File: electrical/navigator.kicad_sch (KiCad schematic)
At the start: 10 parts

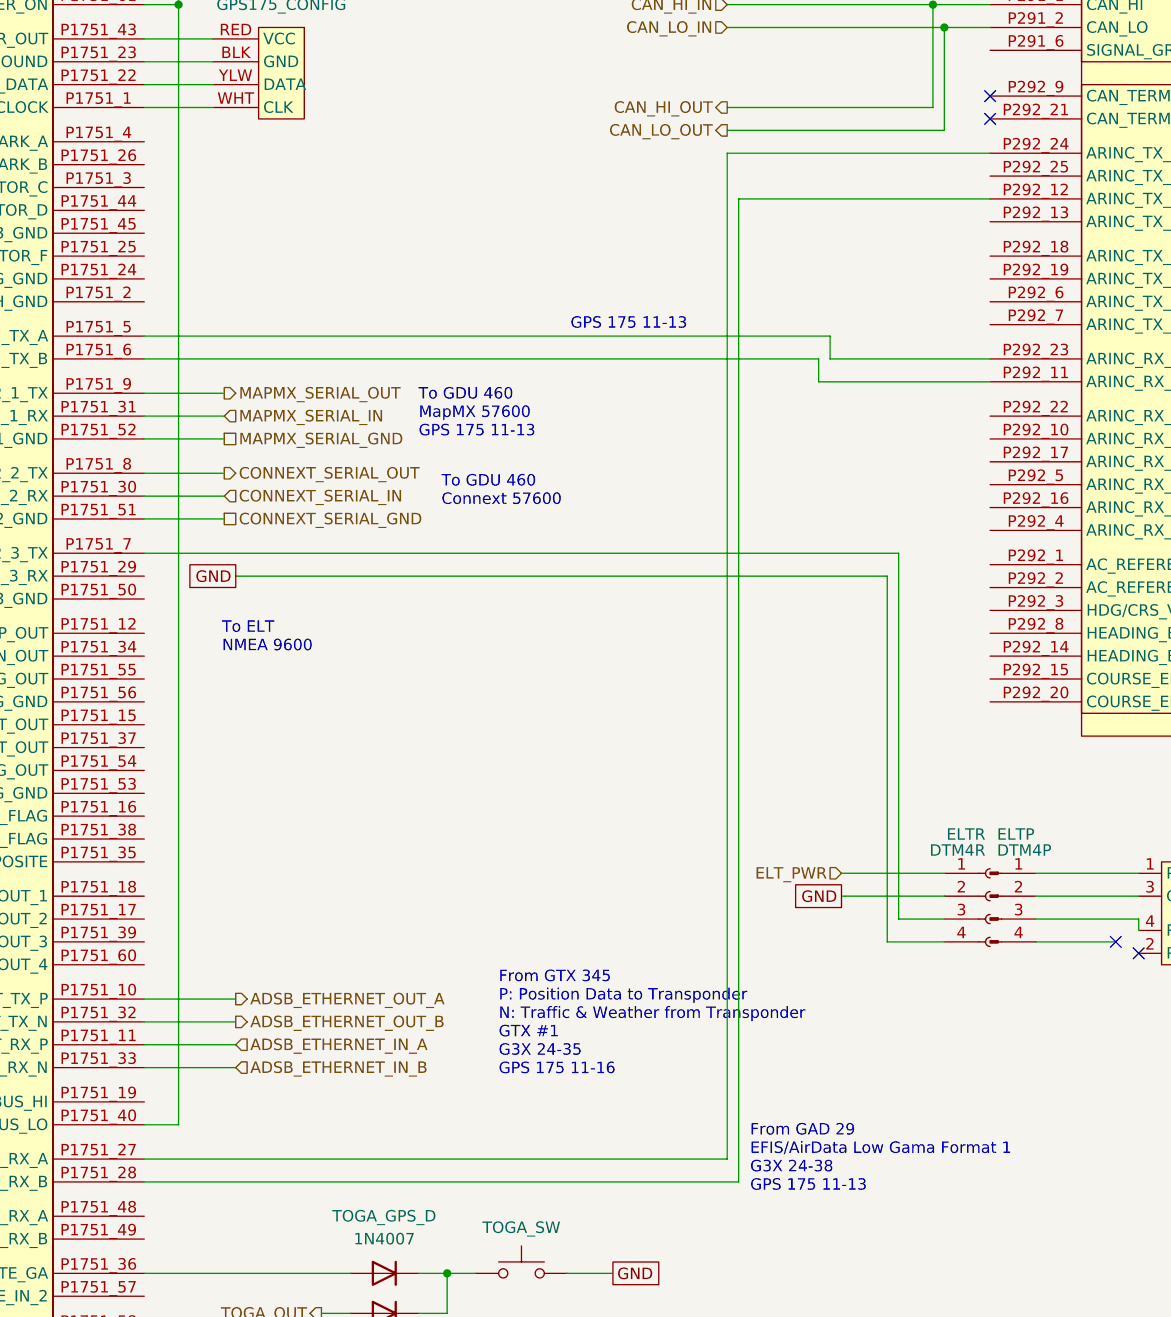
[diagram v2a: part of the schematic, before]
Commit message: Added RS232 and Canbus wiring notation
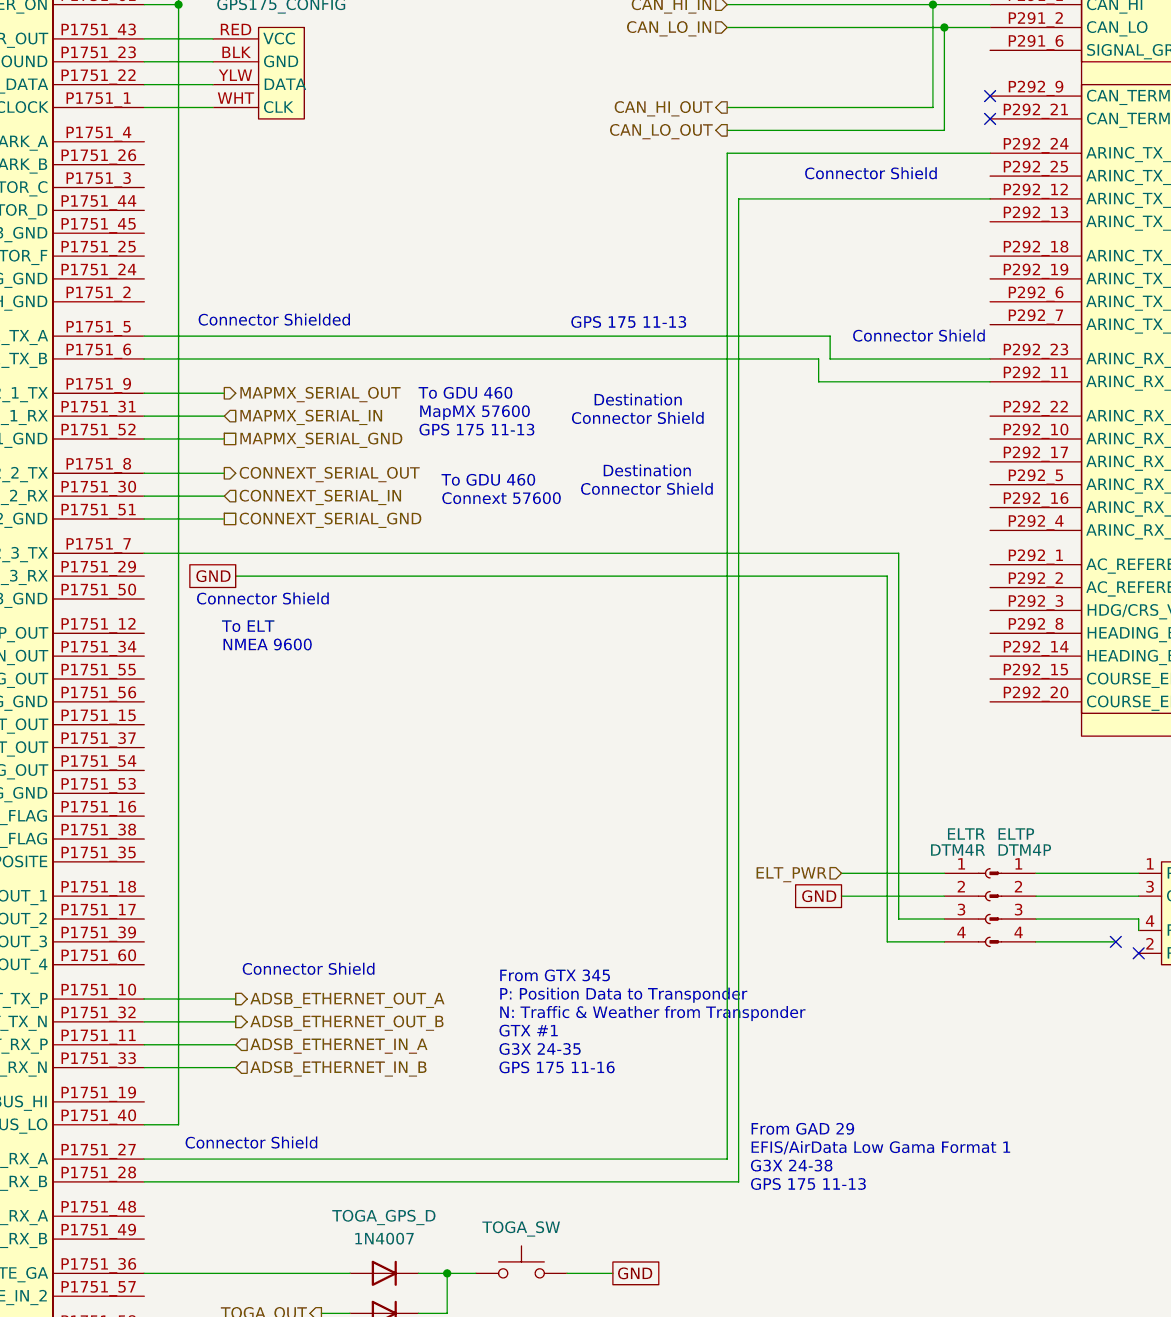
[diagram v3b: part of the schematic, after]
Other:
- note added: "Connector Shield"
- note added: "Connector Shielded"
- note added: "Destination Connector Shield"
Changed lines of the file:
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@@
 	(paper "USLetter" portrait)
 	(title_block
-		(date "2025-10-01")
-		(rev "1.1")
+		(date "2025-10-02")
+		(rev "1.1.4")
 		(company "N78HR")
 	)
@@
 		)
 	)
+	(text "Connector Shield"
+		(exclude_from_sim no)
+		(at 83.058 139.192 0)
+		(effects
+			(font
+				(size 1.27 1.27)
+			)
+		)
+	)
 	(text "To GDU 460\nConnext 57600"
 		(exclude_from_sim no)
@@
 			)
 			(justify left bottom)
+		)
+	)
+	(text "Connector Shield"
+		(exclude_from_sim no)
+		(at 77.978 98.044 0)
+		(effects
+			(font
+				(size 1.27 1.27)
+			)
+		)
+	)
+	(text "Connector Shield"
+		(exclude_from_sim no)
+		(at 150.876 68.834 0)
+		(effects
+			(font
+				(size 1.27 1.27)
+			)
+		)
+	)
+	(text "Destination\nConnector Shield"
+		(exclude_from_sim no)
+		(at 119.634 76.962 0)
+		(effects
+			(font
+				(size 1.27 1.27)
+			)
+		)
+	)
+	(text "Connector Shield"
+		(exclude_from_sim no)
+		(at 76.708 158.496 0)
+		(effects
+			(font
+				(size 1.27 1.27)
+			)
 		)
 	)
@@
 		)
 	)
+	(text "Destination\nConnector Shield"
+		(exclude_from_sim no)
+		(at 120.65 84.836 0)
+		(effects
+			(font
+				(size 1.27 1.27)
+			)
+		)
+	)
 	(text "From GAD 29\nEFIS/AirData Low Gama Format 1\nG3X 24-38\nGPS 175 11-13"
 		(exclude_from_sim no)
@@
 			)
 			(justify left bottom)
+		)
+	)
+	(text "Connector Shielded"
+		(exclude_from_sim no)
+		(at 79.248 67.056 0)
+		(effects
+			(font
+				(size 1.27 1.27)
+			)
 		)
 	)
@@
 		)
 	)
+	(text "Connector Shield"
+		(exclude_from_sim no)
+		(at 145.542 50.8 0)
+		(effects
+			(font
+				(size 1.27 1.27)
+			)
+		)
+	)

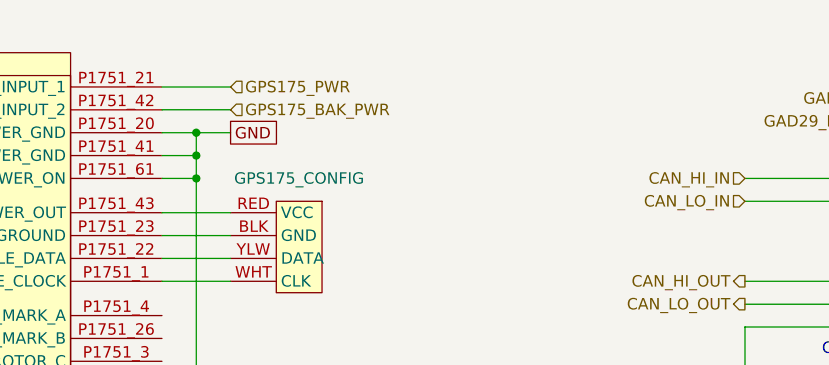
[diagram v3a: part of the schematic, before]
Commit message: Added diode to GPS 175 backup power.
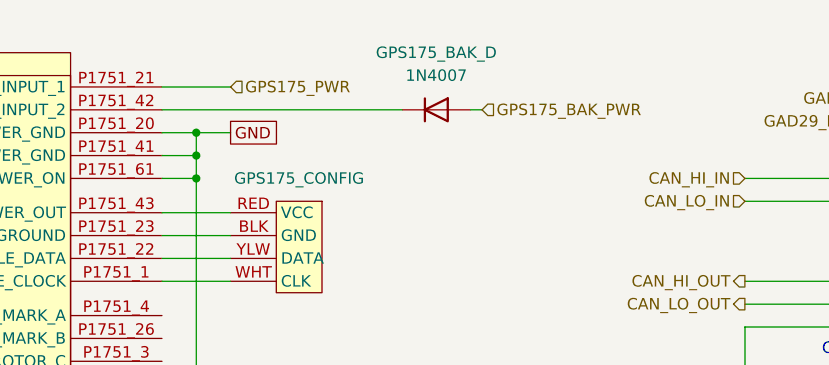
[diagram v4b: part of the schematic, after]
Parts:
- added GPS175_BAK_D: 1N4007, Diode_THT:D_DO-41_SOD81_P10.16mm_Horizontal, symbol Diode:1N4007
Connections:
- net GPS175_BAK_PWR: now also GPS175_BAK_D.2 (A); no longer GPS175.P1751_42 (POWER_INPUT_2)
- new net: GPS175.P1751_42 (POWER_INPUT_2), GPS175_BAK_D.1 (K)
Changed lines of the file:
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@@
 	(paper "USLetter" portrait)
 	(title_block
-		(date "2025-10-02")
-		(rev "1.1.4")
+		(date "2025-10-10")
+		(rev "1.1.6")
 		(company "N78HR")
 	)
@@
 	(wire
 		(pts
-			(xy 64.77 24.13) (xy 72.39 24.13)
-		)
-		(stroke
-			(width 0)
-			(type default)
-		)
-	)
-	(wire
-		(pts
 			(xy 64.77 74.93) (xy 73.66 74.93)
 		)
@@
 	(wire
 		(pts
+			(xy 64.77 24.13) (xy 91.44 24.13)
+		)
+		(stroke
+			(width 0)
+			(type default)
+		)
+	)
+	(wire
+		(pts
 			(xy 64.77 31.75) (xy 68.58 31.75)
 		)
@@
 		(pts
 			(xy 64.77 26.67) (xy 68.58 26.67)
+		)
+		(stroke
+			(width 0)
+			(type default)
+		)
+	)
+	(wire
+		(pts
+			(xy 99.06 24.13) (xy 100.33 24.13)
 		)
 		(stroke
@@
 	(hierarchical_label "GPS175_BAK_PWR"
 		(shape input)
-		(at 72.39 24.13 0)
+		(at 100.33 24.13 0)
 		(effects
 			(font
@@
 					(unit 1)
 				)
+			)
+		)
+	)
+	(symbol
+		(lib_id "Diode:1N4007")
+		(at 95.25 24.13 0)
+		(unit 1)
+		(exclude_from_sim no)
+		(in_bom yes)
+		(on_board yes)
+		(dnp no)
+		(property "Reference" "GPS175_BAK_D"
+			(at 95.25 17.78 0)
+			(effects
+				(font
+					(size 1.27 1.27)
+				)
+			)
+		)
+		(property "Value" "1N4007"
+			(at 95.25 20.32 0)
+			(effects
+				(font
+					(size 1.27 1.27)
+				)
+			)
+		)
+		(property "Footprint" "Diode_THT:D_DO-41_SOD81_P10.16mm_Horizontal"
+			(at 95.25 28.575 0)
+			(effects
+				(font
+					(size 1.27 1.27)
+				)
+				(hide yes)
+			)
+		)
+		(property "Datasheet" "http://www.vishay.com/docs/88503/1n4001.pdf"
+			(at 95.25 24.13 0)
+			(effects
+				(font
+					(size 1.27 1.27)
+				)
+				(hide yes)
+			)
+		)
+		(property "Description" ""
+			(at 95.25 24.13 0)
+			(effects
+				(font
+					(size 1.27 1.27)
+				)
+			)
+		)
+		(property "Sim.Device" "D"
+			(at 95.25 24.13 0)
+			(effects
+				(font
+					(size 1.27 1.27)
+				)
+				(hide yes)
+			)
+		)
+		(property "Sim.Pins" "1=K 2=A"
+			(at 95.25 24.13 0)
+			(effects
+				(font
+					(size 1.27 1.27)
+				)
+				(hide yes)
+			)
+		)
+		(pin "2"
+		)
+		(pin "1"
+		)
+		(instances
+			(project "electrical"
+				(path "/e8ec215a-dbe2-4eba-a577-e50a0a128049/a7d1a714-f940-4397-adef-d76b5058aa57"
+					(reference "GPS175_BAK_D")
+					(unit 1)
+				)

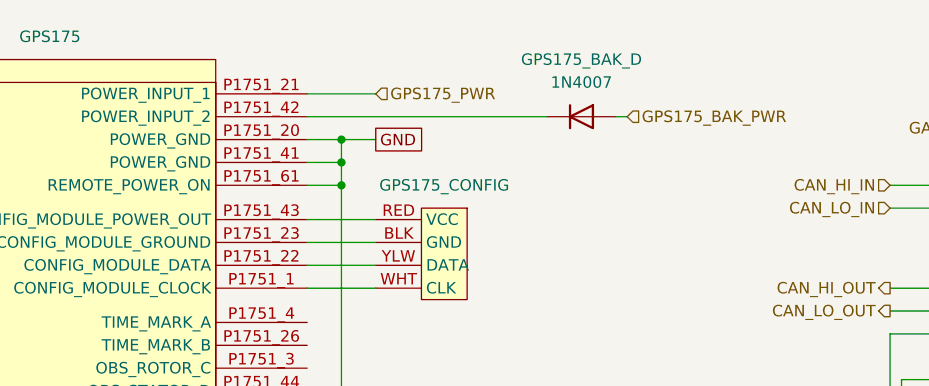
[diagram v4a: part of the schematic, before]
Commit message: Added a diode on the power side for the GPS 175 as it's connected internally, which I didn't expect. This is to prevent backfeeding between AV power and backup power.
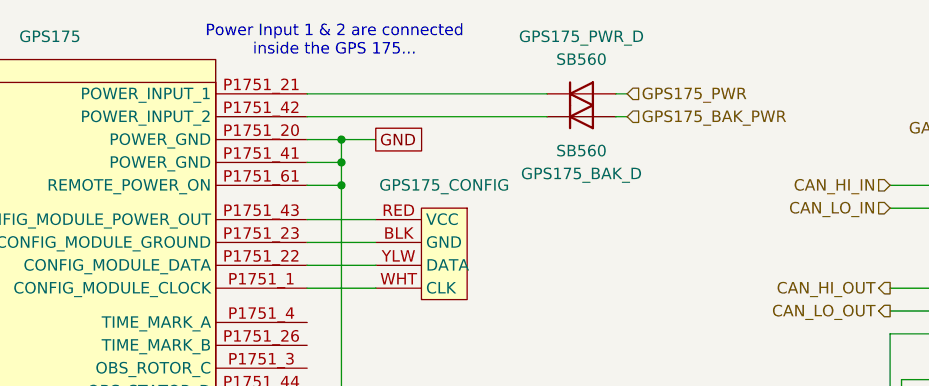
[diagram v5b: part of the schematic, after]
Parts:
- added GPS175_PWR_D: SB560, Diode_THT:D_DO-41_SOD81_P10.16mm_Horizontal, symbol Diode:1N4007
- GPS175_BAK_D: value 1N4007 -> SB560
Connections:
- net GPS175_PWR: now also GPS175_PWR_D.2 (A); no longer GPS175.P1751_21 (POWER_INPUT_1)
- new net: GPS175.P1751_21 (POWER_INPUT_1), GPS175_PWR_D.1 (K)
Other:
- note added: "Power Input 1 & 2 are connected inside the GPS 175..."
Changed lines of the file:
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@@
 	(paper "USLetter" portrait)
 	(title_block
-		(date "2025-10-10")
-		(rev "1.1.6")
+		(date "2025-10-11")
+		(rev "1.1.7")
 		(company "N78HR")
 	)
@@
 		(exclude_from_sim no)
 		(at 120.65 84.836 0)
+		(effects
+			(font
+				(size 1.27 1.27)
+			)
+		)
+	)
+	(text "Power Input 1 & 2 are connected\ninside the GPS 175..."
+		(exclude_from_sim no)
+		(at 67.818 15.748 0)
 		(effects
 			(font
@@
 	(wire
 		(pts
-			(xy 64.77 21.59) (xy 72.39 21.59)
+			(xy 99.06 21.59) (xy 100.33 21.59)
 		)
 		(stroke
@@
 		(pts
 			(xy 152.4 31.75) (xy 158.75 31.75)
+		)
+		(stroke
+			(width 0)
+			(type default)
+		)
+	)
+	(wire
+		(pts
+			(xy 91.44 21.59) (xy 64.77 21.59)
 		)
 		(stroke
@@
 	(hierarchical_label "GPS175_PWR"
 		(shape input)
-		(at 72.39 21.59 0)
+		(at 100.33 21.59 0)
 		(effects
 			(font
@@
 				(path "/e8ec215a-dbe2-4eba-a577-e50a0a128049/a7d1a714-f940-4397-adef-d76b5058aa57"
 					(reference "ELTP")
+					(unit 1)
+				)
+			)
+		)
+	)
+	(symbol
+		(lib_id "Diode:1N4007")
+		(at 95.25 21.59 0)
+		(unit 1)
+		(exclude_from_sim no)
+		(in_bom yes)
+		(on_board yes)
+		(dnp no)
+		(property "Reference" "GPS175_PWR_D"
+			(at 95.25 15.24 0)
+			(effects
+				(font
+					(size 1.27 1.27)
+				)
+			)
+		)
+		(property "Value" "SB560"
+			(at 95.25 17.78 0)
+			(effects
+				(font
+					(size 1.27 1.27)
+				)
+			)
+		)
+		(property "Footprint" "Diode_THT:D_DO-41_SOD81_P10.16mm_Horizontal"
+			(at 95.25 26.035 0)
+			(effects
+				(font
+					(size 1.27 1.27)
+				)
+				(hide yes)
+			)
+		)
+		(property "Datasheet" "http://www.vishay.com/docs/88503/1n4001.pdf"
+			(at 95.25 21.59 0)
+			(effects
+				(font
+					(size 1.27 1.27)
+				)
+				(hide yes)
+			)
+		)
+		(property "Description" ""
+			(at 95.25 21.59 0)
+			(effects
+				(font
+					(size 1.27 1.27)
+				)
+			)
+		)
+		(property "Sim.Device" "D"
+			(at 95.25 21.59 0)
+			(effects
+				(font
+					(size 1.27 1.27)
+				)
+				(hide yes)
+			)
+		)
+		(property "Sim.Pins" "1=K 2=A"
+			(at 95.25 21.59 0)
+			(effects
+				(font
+					(size 1.27 1.27)
+				)
+				(hide yes)
+			)
+		)
+		(pin "2"
+		)
+		(pin "1"
+		)
+		(instances
+			(project "electrical"
+				(path "/e8ec215a-dbe2-4eba-a577-e50a0a128049/a7d1a714-f940-4397-adef-d76b5058aa57"
+					(reference "GPS175_PWR_D")
 					(unit 1)
 				)
@@
 		(lib_id "Diode:1N4007")
 		(at 95.25 24.13 0)
+		(mirror x)
 		(unit 1)
 		(exclude_from_sim no)
@@
 		(dnp no)
 		(property "Reference" "GPS175_BAK_D"
-			(at 95.25 17.78 0)
-			(effects
-				(font
-					(size 1.27 1.27)
-				)
-			)
-		)
-		(property "Value" "1N4007"
-			(at 95.25 20.32 0)
+			(at 95.25 30.48 0)
+			(effects
+				(font
+					(size 1.27 1.27)
+				)
+			)
+		)
+		(property "Value" "SB560"
+			(at 95.25 27.94 0)
 			(effects
 				(font
@@
 		)
 		(property "Footprint" "Diode_THT:D_DO-41_SOD81_P10.16mm_Horizontal"
-			(at 95.25 28.575 0)
-			(effects
-				(font
+			(at 95.25 19.685 0)
+			(effects
+				(font

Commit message: Added lighting bus
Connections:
- net GND: no longer GPS175.P1751_40 (LIGHTING_BUS_LO)
- net LIGHTS_HI: now reaches GPS175.P1751_19 (LIGHTING_BUS_HI)
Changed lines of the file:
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@@
 	(paper "USLetter" portrait)
 	(title_block
-		(date "2025-10-11")
-		(rev "1.1.7")
+		(date "2025-10-19")
+		(rev "1.1.15")
 		(company "N78HR")
 	)
@@
 			)
 		)
-	)
-	(junction
-		(at 68.58 31.75)
-		(diameter 0)
-		(color 0 0 0 0)
 	)
 	(junction
@@
 	(wire
 		(pts
-			(xy 64.77 156.21) (xy 68.58 156.21)
-		)
-		(stroke
-			(width 0)
-			(type default)
-		)
-	)
-	(wire
-		(pts
 			(xy 68.58 26.67) (xy 72.39 26.67)
 		)
@@
 	(wire
 		(pts
+			(xy 64.77 153.67) (xy 74.93 153.67)
+		)
+		(stroke
+			(width 0)
+			(type default)
+		)
+	)
+	(wire
+		(pts
 			(xy 130.81 53.34) (xy 158.75 53.34)
 		)
@@
 		(pts
 			(xy 64.77 71.12) (xy 139.7 71.12)
-		)
-		(stroke
-			(width 0)
-			(type default)
-		)
-	)
-	(wire
-		(pts
-			(xy 68.58 156.21) (xy 68.58 31.75)
 		)
 		(stroke
@@
 		)
 	)
+	(hierarchical_label "LIGHTS_HI"
+		(shape input)
+		(at 74.93 153.67 0)
+		(effects
+			(font
+				(size 1.27 1.27)
+			)
+			(justify left)
+		)
+	)

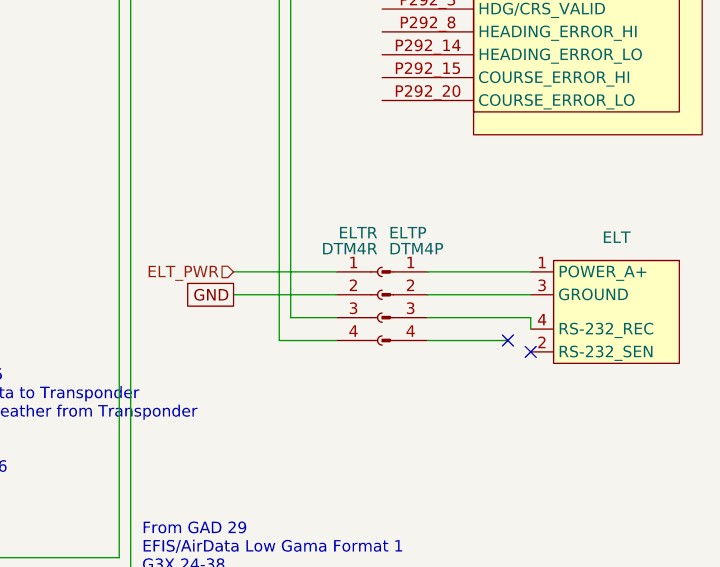
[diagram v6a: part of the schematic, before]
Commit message: Corrected all rececptacle/plug polarity and naming.
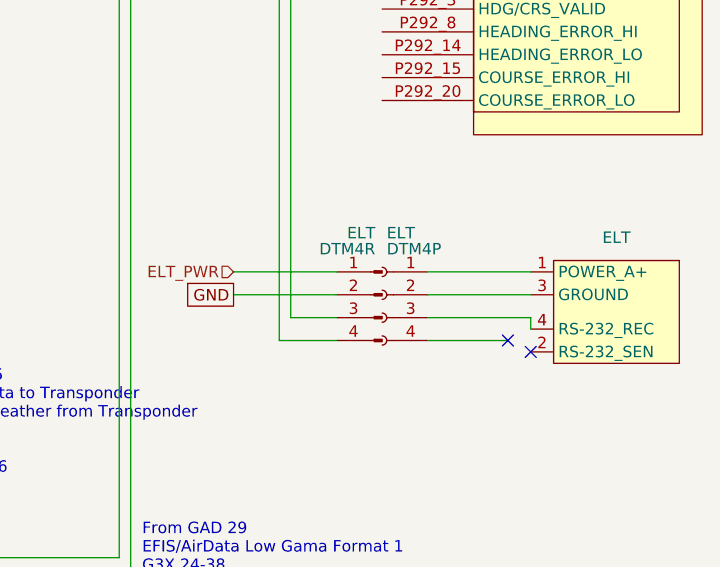
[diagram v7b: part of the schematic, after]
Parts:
- ELT: renamed from ELTR; value DTM4R -> DTM4P
- ELT: renamed from ELTP; value DTM4P -> DTM4R
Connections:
- net ELT_PWR: now also ELT.1 (Pin_1); no longer ELT.1 (Pin_1)
- net GND: now also ELT.2 (Pin_2), ELT.4 (Pin_4); no longer ELT.2 (Pin_2), ELT.4 (Pin_4)
- net at ELT.3 (Pin_3): now also ELT.4 (RS-232_REC); no longer GPS175.P1751_7 (RS-232_3_TX)
- net at ELT.1 (POWER_A+): now also ELT.1 (Pin_1); no longer ELT.1 (Pin_1)
- net at ELT.3 (GROUND): now also ELT.2 (Pin_2); no longer ELT.2 (Pin_2)
- net at ELT.3 (Pin_3): now also GPS175.P1751_7 (RS-232_3_TX); no longer ELT.4 (RS-232_REC)
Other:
- moved on the sheet: ELT
